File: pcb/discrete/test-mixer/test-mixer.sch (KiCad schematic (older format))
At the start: 77 parts, among them J1 UFL, J2 UFL, J3 SMA, J4 Conn_01x08, J5 Conn_01x01, J6 Conn_01x01, T1 HHM17147A1, T2 HHM17147A1, U1 ADF4360-7BCPZ, U2 BAT15-099R, X1 EC5-5032MV-100-BN-TR

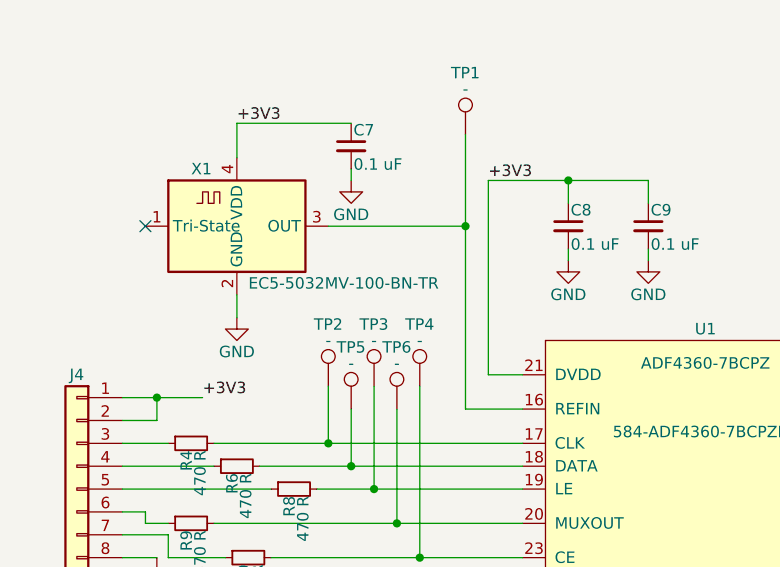
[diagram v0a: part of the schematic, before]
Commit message: Add in some more footprints before autofill
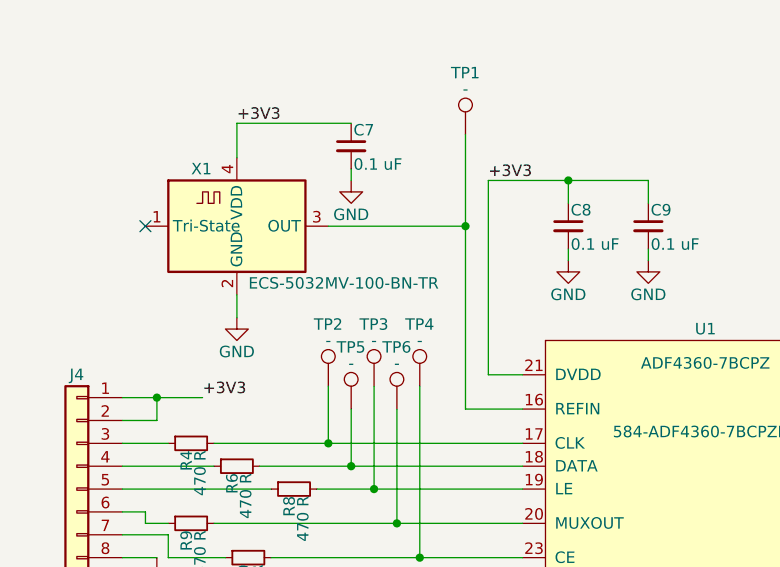
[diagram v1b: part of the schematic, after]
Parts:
- C10, C11, C2, C3, C4: footprint (none) -> Capacitor_SMD:C_0603_1608Metric_Pad1.05x0.95mm_HandSolder; Mouser (none) -> 791-RF18N101J500CT
- C12, C13, C21, C6: footprint (none) -> Capacitor_SMD:C_0402_1005Metric; Mouser (none) -> 80-C0402C103K4R7411
- C16, L10, L11, L12, L5, L6, L7, L9: footprint (none) -> Capacitor_SMD:C_0402_1005Metric; Mouser (none) -> NoPart
- C17: footprint (none) -> Capacitor_SMD:C_0402_1005Metric; Mouser (none) -> 81-GJM1555C1H3R9CB1D
- C8, C9: footprint (none) -> Capacitor_SMD:C_0402_1005Metric; Mouser (none) -> 80-C0402C104M4P
- J2: footprint (none) -> discrete_footprints:2337019-1; Mouser (none) -> 571-2337019-1
- J6: footprint (none) -> Connector_PinSocket_2.54mm:PinSocket_1x01_P2.54mm_Vertical; Mouser (none) -> NoPart
- L15: footprint (none) -> Capacitor_SMD:C_0402_1005Metric; Mouser (none) -> 815-AIML-0402-1R0KT
- L17: footprint (none) -> Capacitor_SMD:C_0402_1005Metric; Mouser (none) -> 81-LQG15HS3N9C02D
- L2: footprint (none) -> Capacitor_SMD:C_0402_1005Metric; Mouser (none) -> 81-LQG15HZ47NJ02D
- L8: footprint (none) -> Capacitor_SMD:C_0402_1005Metric; Mouser (none) -> 81-LQG15HN7N5J02D
- R10, R16, R17, R6, R8, R9: footprint (none) -> Resistor_SMD:R_0402_1005Metric; Mouser (none) -> 603-RC0402JR-13470RL
- R12, R15, R5: footprint (none) -> Resistor_SMD:R_0402_1005Metric; Mouser (none) -> NoPart
- R2: footprint (none) -> Resistor_SMD:R_0603_1608Metric_Pad1.05x0.95mm_HandSolder; Mouser (none) -> 652-CR0603-J/-3R3ELF
- R7: footprint (none) -> Resistor_SMD:R_0402_1005Metric; Mouser (none) -> 71-CRCW04020000Z0EDC
- T1: footprint (none) -> discrete_footprints:TDK_HHM17147A1
- TP1, TP3, TP4, TP5, TP6, TP7, TP8, TP9: footprint (none) -> TestPoint:TestPoint_Pad_D1.0mm; Mouser (none) -> NoPart
- X1: value EC5-5032MV-100-BN-TR -> ECS-5032MV-100-BN-TR; Mouser (none) -> 520-5032MV-100-BNT

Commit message: Autofill finish
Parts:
- L13, L14: footprint (none) -> Capacitor_SMD:C_0402_1005Metric; Mouser (none) -> 815-AIML-0402-1R0KT
- T2: footprint (none) -> discrete_footprints:TDK_HHM17147A1
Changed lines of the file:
@@
 F 0 "T2" H 9900 4150 50  0000 C CNN
 F 1 "HHM17147A1" H 9900 3650 50  0000 C CNN
-F 2 "" H 9900 4150 50  0001 C CNN
+F 2 "discrete_footprints:TDK_HHM17147A1" H 9900 4150 50  0001 C CNN
 F 3 "" H 9900 4150 50  0001 C CNN
 F 4 "810-HHM17147A1" H 9900 3550 50  0000 C CNN "Mouser"
@@
 F 0 "L14" H 6280 4340 50  0000 L CNN
 F 1 "1 uH" H 6280 4260 50  0000 L CNN
-F 2 "" H 6250 4300 50  0001 C CNN
+F 2 "Capacitor_SMD:C_0402_1005Metric" H 6250 4300 50  0001 C CNN
 F 3 "~" H 6250 4300 50  0001 C CNN
+F 4 "815-AIML-0402-1R0KT" H 6250 4300 50  0001 C CNN "Mouser"
 	1    6250 4300
 	-1   0    0    -1
@@
 F 0 "L13" H 9630 4290 50  0000 L CNN
 F 1 "1 uH" H 9630 4210 50  0000 L CNN
-F 2 "" H 9600 4250 50  0001 C CNN
+F 2 "Capacitor_SMD:C_0402_1005Metric" H 9600 4250 50  0001 C CNN
 F 3 "~" H 9600 4250 50  0001 C CNN
+F 4 "815-AIML-0402-1R0KT" H 9600 4250 50  0001 C CNN "Mouser"
 	1    9600 4250
 	1    0    0    -1

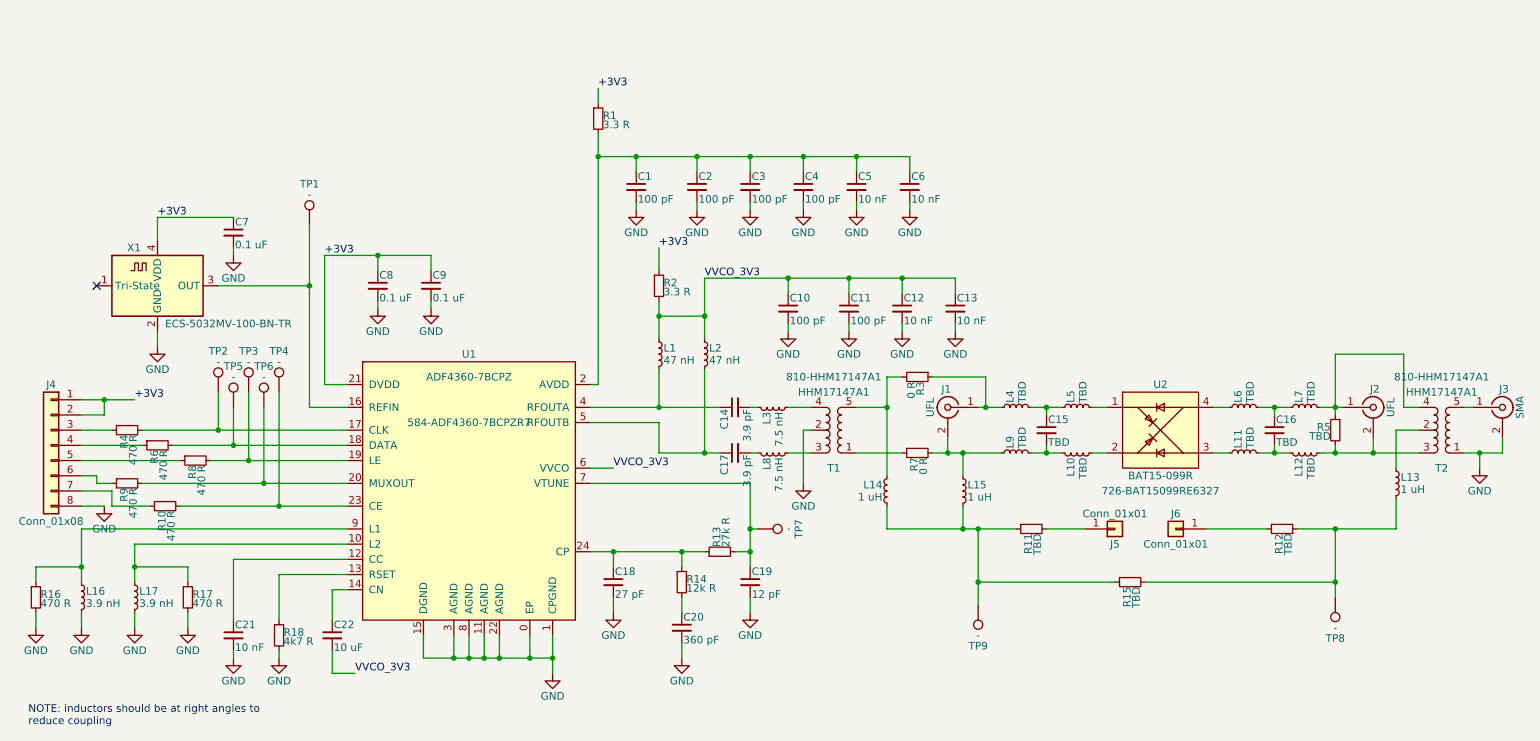
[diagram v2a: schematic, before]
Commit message: Add mounting holes, fix DRC errors
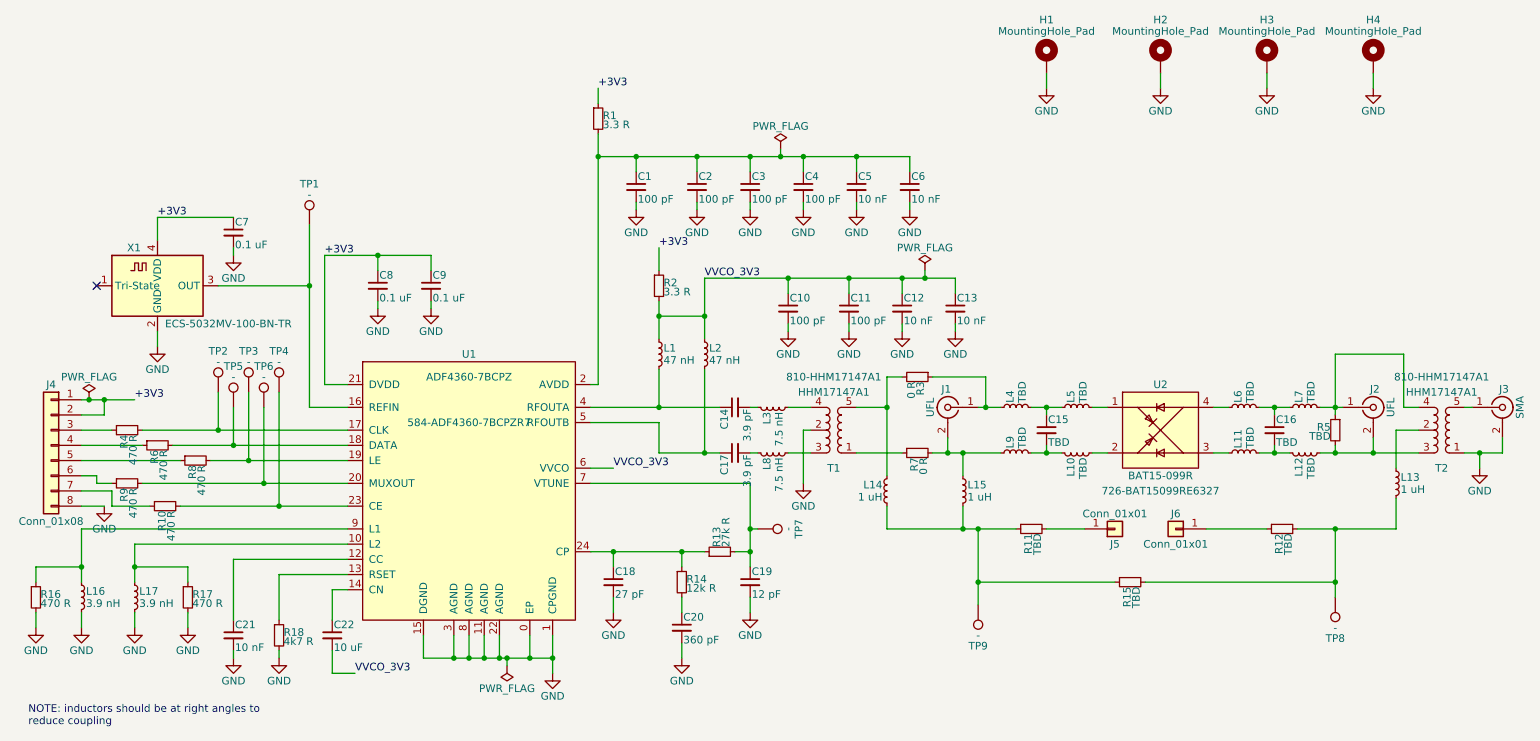
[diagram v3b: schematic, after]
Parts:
- added H1, H2, H3, H4: MountingHole_Pad, MountingHole:MountingHole_3.2mm_M3_DIN965, symbol Mechanical:MountingHole_Pad
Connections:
- net GND: now also H1.1, H2.1, H3.1, H4.1
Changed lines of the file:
@@
 	3700 5250 3700 5400
 Wire Wire Line
-	3700 5400 3900 5400
+	3700 5400 3750 5400
 Connection ~ 3900 5400
 Wire Wire Line
@@
 $EndComp
 Wire Wire Line
-	6350 2900 6700 2900
+	6350 2900 6500 2900
 Wire Wire Line
 	6700 2900 6700 3000
@@
 Connection ~ 5350 2100
 Wire Wire Line
-	5350 2100 5700 2100
+	5350 2100 5550 2100
 Wire Wire Line
 	5000 2100 5000 2200
@@
 Connection ~ 1100 3700
 Wire Wire Line
-	1100 3700 950  3700
+	1100 3700 1000 3700
 Text Label 1300 3700 0    50   ~ 0
 +3V3
@@
 Wire Wire Line
 	9200 3800 9200 3750
+$Comp
+L power:PWR_FLAG #FLG01
+U 1 1 5E1A9D94
+P 1000 3700
+F 0 "#FLG01" H 1000 3775 50  0001 C CNN
+F 1 "PWR_FLAG" H 1000 3850 50  0000 C CNN
+F 2 "" H 1000 3700 50  0001 C CNN
+F 3 "~" H 1000 3700 50  0001 C CNN
+	1    1000 3700
+	1    0    0    -1
+$EndComp
+Connection ~ 1000 3700
+Wire Wire Line
+	1000 3700 950  3700
+Wire Wire Line
+	3750 5450 3750 5400
+Connection ~ 3750 5400
+Wire Wire Line
+	3750 5400 3900 5400
+$Comp
+L power:PWR_FLAG #FLG02
+U 1 1 5E1C9779
+P 5550 2050
+F 0 "#FLG02" H 5550 2125 50  0001 C CNN
+F 1 "PWR_FLAG" H 5550 2200 50  0000 C CNN
+F 2 "" H 5550 2050 50  0001 C CNN
+F 3 "~" H 5550 2050 50  0001 C CNN
+	1    5550 2050
+	1    0    0    -1
+$EndComp
+$Comp
+L power:PWR_FLAG #FLG03
+U 1 1 5E1C9F6C
+P 6500 2850
+F 0 "#FLG03" H 6500 2925 50  0001 C CNN
+F 1 "PWR_FLAG" H 6500 3000 50  0000 C CNN
+F 2 "" H 6500 2850 50  0001 C CNN
+F 3 "~" H 6500 2850 50  0001 C CNN
+	1    6500 2850
+	1    0    0    -1
+$EndComp
+Wire Wire Line
+	5550 2050 5550 2100
+Connection ~ 5550 2100
+Wire Wire Line
+	5550 2100 5700 2100
+Wire Wire Line
+	6500 2850 6500 2900
+Connection ~ 6500 2900
+Wire Wire Line
+	6500 2900 6700 2900
+$Comp
+L Mechanical:MountingHole_Pad H1
+U 1 1 5E1EC3F2
+P 7300 1450
+F 0 "H1" H 7300 1700 50  0000 C CNN
+F 1 "MountingHole_Pad" H 7300 1625 50  0000 C CNN
+F 2 "MountingHole:MountingHole_3.2mm_M3_DIN965" H 7300 1450 50  0001 C CNN
+F 3 "~" H 7300 1450 50  0001 C CNN
+F 4 "NoPart" H 7300 1450 50  0001 C CNN "Mouser"
+	1    7300 1450
+	1    0    0    -1
+$EndComp
+$Comp
+L power:GND #PWR029
+U 1 1 5E1EED1B
+P 7300 1650
+F 0 "#PWR029" H 7300 1400 50  0001 C CNN
+F 1 "GND" H 7300 1500 50  0000 C CNN
+F 2 "" H 7300 1650 50  0001 C CNN
+F 3 "" H 7300 1650 50  0001 C CNN
+	1    7300 1650
+	1    0    0    -1
+$EndComp
+Wire Wire Line
+	7300 1650 7300 1550
+$Comp
+L Mechanical:MountingHole_Pad H2
+U 1 1 5E200292
+P 8050 1450
+F 0 "H2" H 8050 1700 50  0000 C CNN
+F 1 "MountingHole_Pad" H 8050 1625 50  0000 C CNN
+F 2 "MountingHole:MountingHole_3.2mm_M3_DIN965" H 8050 1450 50  0001 C CNN
+F 3 "~" H 8050 1450 50  0001 C CNN
+F 4 "NoPart" H 8050 1450 50  0001 C CNN "Mouser"
+	1    8050 1450
+	1    0    0    -1
+$EndComp
+$Comp
+L power:GND #PWR030
+U 1 1 5E200298
+P 8050 1650
+F 0 "#PWR030" H 8050 1400 50  0001 C CNN
+F 1 "GND" H 8050 1500 50  0000 C CNN
+F 2 "" H 8050 1650 50  0001 C CNN
+F 3 "" H 8050 1650 50  0001 C CNN
+	1    8050 1650
+	1    0    0    -1
+$EndComp
+Wire Wire Line
+	8050 1650 8050 1550
+$Comp
+L Mechanical:MountingHole_Pad H3
+U 1 1 5E210963
+P 8750 1450
+F 0 "H3" H 8750 1700 50  0000 C CNN
+F 1 "MountingHole_Pad" H 8750 1625 50  0000 C CNN
+F 2 "MountingHole:MountingHole_3.2mm_M3_DIN965" H 8750 1450 50  0001 C CNN
+F 3 "~" H 8750 1450 50  0001 C CNN
+F 4 "NoPart" H 8750 1450 50  0001 C CNN "Mouser"
+	1    8750 1450
+	1    0    0    -1
+$EndComp
+$Comp
+L power:GND #PWR031
+U 1 1 5E210969
+P 8750 1650
+F 0 "#PWR031" H 8750 1400 50  0001 C CNN
+F 1 "GND" H 8750 1500 50  0000 C CNN
+F 2 "" H 8750 1650 50  0001 C CNN
+F 3 "" H 8750 1650 50  0001 C CNN
+	1    8750 1650
+	1    0    0    -1
+$EndComp
+Wire Wire Line
+	8750 1650 8750 1550
+$Comp
+L Mechanical:MountingHole_Pad H4
+U 1 1 5E220F89
+P 9450 1450
+F 0 "H4" H 9450 1700 50  0000 C CNN
+F 1 "MountingHole_Pad" H 9450 1625 50  0000 C CNN
+F 2 "MountingHole:MountingHole_3.2mm_M3_DIN965" H 9450 1450 50  0001 C CNN
+F 3 "~" H 9450 1450 50  0001 C CNN
+F 4 "NoPart" H 9450 1450 50  0001 C CNN "Mouser"
+	1    9450 1450
+	1    0    0    -1
+$EndComp
+$Comp
+L power:GND #PWR032
+U 1 1 5E220F8F
+P 9450 1650
+F 0 "#PWR032" H 9450 1400 50  0001 C CNN
+F 1 "GND" H 9450 1500 50  0000 C CNN
+F 2 "" H 9450 1650 50  0001 C CNN
+F 3 "" H 9450 1650 50  0001 C CNN
+	1    9450 1650
+	1    0    0    -1
+$EndComp
+Wire Wire Line
+	9450 1650 9450 1550
+$Comp
+L power:PWR_FLAG #FLG0101
+U 1 1 5E2386E0
+P 3750 5450
+F 0 "#FLG0101" H 3750 5525 50  0001 C CNN
+F 1 "PWR_FLAG" H 3750 5600 50  0000 C CNN
+F 2 "" H 3750 5450 50  0001 C CNN
+F 3 "~" H 3750 5450 50  0001 C CNN
+	1    3750 5450
+	-1   0    0    1
+$EndComp
 $EndSCHEMATC

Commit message: Finish layout
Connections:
- net GND: now also T2.5 (GND); no longer T2.1 (SINGLE)
- net LO_OUT_P: now reaches C14.1, L1.2, U1.4 (RFOUTA)
- net LO_OUT_N: now reaches C17.1, L2.2, U1.5 (RFOUTB)
- net at U2.1 (A): now also L10.2; no longer L5.2
- net at U2.2 (B): now also L5.2; no longer L10.2
- net at U2.3 (C): now also L6.1; no longer L11.1
- net at U2.4 (D): now also L11.1; no longer L6.1
- net RF: now reaches J3.1 (In)
- net RF: now also T2.1 (SINGLE); no longer T2.5 (GND)
- net at J1.2 (Ext), L9.1, R7.2: no longer L15.1
- net LO_BAL_P: now reaches L14.1, R3.2, T1.5 (GND)
- net LO_BAL_N: now reaches R7.1, T1.1 (SINGLE)
- net LO_BAL_N: now also L15.1
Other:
- moved on the sheet: J3, L14, L15
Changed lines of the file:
@@
 F 4 "726-BAT15099RE6327" H 8050 3500 50  0000 C CNN "Mouser"
 	1    8050 3900
-	1    0    0    -1
+	1    0    0    1
 $EndComp
 $Comp
@@
 L Connector:Conn_Coaxial J3
 U 1 1 5DAA7992
-P 10300 3750
-F 0 "J3" H 10310 3870 50  0000 C CNN
-F 1 "SMA" V 10415 3750 50  0000 C CNN
-F 2 "discrete_footprints:142-0701-801-with-taper" H 10300 3750 50  0001 C CNN
-F 3 " ~" H 10300 3750 50  0001 C CNN
-F 4 " 530-142-0701-801 " H 10300 3750 50  0001 C CNN "Mouser"
-	1    10300 3750
-	1    0    0    -1
+P 10300 4050
+F 0 "J3" H 10310 4170 50  0000 C CNN
+F 1 "SMA" V 10415 4050 50  0000 C CNN
+F 2 "discrete_footprints:142-0701-801-with-taper" H 10300 4050 50  0001 C CNN
+F 3 " ~" H 10300 4050 50  0001 C CNN
+F 4 " 530-142-0701-801 " H 10300 4050 50  0001 C CNN "Mouser"
+	1    10300 4050
+	1    0    0    1
 $EndComp
 $Comp
@@
 F 4 "815-AIML-0402-1R0KT" H 6250 4300 50  0001 C CNN "Mouser"
 	1    6250 4300
-	-1   0    0    -1
+	1    0    0    -1
 $EndComp
 $Comp
 L Device:L_Small L15
 U 1 1 5DAB475E
-P 6750 4300
-F 0 "L15" H 6780 4340 50  0000 L CNN
-F 1 "1 uH" H 6780 4260 50  0000 L CNN
-F 2 "Capacitor_SMD:C_0402_1005Metric" H 6750 4300 50  0001 C CNN
-F 3 "~" H 6750 4300 50  0001 C CNN
-F 4 "815-AIML-0402-1R0KT" H 6750 4300 50  0001 C CNN "Mouser"
-	1    6750 4300
-	1    0    0    -1
-$EndComp
-Wire Wire Line
-	6750 4200 6750 4050
-Wire Wire Line
-	6750 4050 7000 4050
+P 6050 4300
+F 0 "L15" H 6080 4340 50  0000 L CNN
+F 1 "1 uH" H 6080 4260 50  0000 L CNN
+F 2 "Capacitor_SMD:C_0402_1005Metric" H 6050 4300 50  0001 C CNN
+F 3 "~" H 6050 4300 50  0001 C CNN
+F 4 "815-AIML-0402-1R0KT" H 6050 4300 50  0001 C CNN "Mouser"
+	1    6050 4300
+	1    0    0    -1
+$EndComp
+Wire Wire Line
+	6050 4200 6050 4050
 Wire Wire Line
 	6250 4200 6250 3750
@@
 Wire Wire Line
 	6650 3950 6650 4050
-Wire Wire Line
-	6650 4050 6750 4050
-Connection ~ 6750 4050
 $Comp
 L Device:C_Small C14
@@
 	6250 4400 6250 4550
 Wire Wire Line
-	6250 4550 6750 4550
-Wire Wire Line
-	6750 4550 6750 4400
+	6050 4550 6050 4400
 $Comp
 L Device:L_Small L13
@@
 	9200 3750 9100 3750
 Wire Wire Line
-	10100 3750 10050 3750
-Wire Wire Line
-	10300 3950 10300 4050
-Wire Wire Line
-	10300 4050 10150 4050
+	10100 4050 10050 4050
+Wire Wire Line
+	10300 3850 10300 3750
+Wire Wire Line
+	10300 3750 10150 3750
 $Comp
 L power:GND #PWR015
 U 1 1 5DAC5ECA
-P 10150 4150
-F 0 "#PWR015" H 10150 3900 50  0001 C CNN
-F 1 "GND" H 10150 4000 50  0000 C CNN
-F 2 "" H 10150 4150 50  0001 C CNN
-F 3 "" H 10150 4150 50  0001 C CNN
-	1    10150 4150
-	1    0    0    -1
-$EndComp
-Wire Wire Line
-	10150 4150 10150 4050
-Connection ~ 10150 4050
-Wire Wire Line
-	10150 4050 10050 4050
+P 10150 3650
+F 0 "#PWR015" H 10150 3400 50  0001 C CNN
+F 1 "GND" H 10150 3500 50  0000 C CNN
+F 2 "" H 10150 3650 50  0001 C CNN
+F 3 "" H 10150 3650 50  0001 C CNN
+	1    10150 3650
+	1    0    0    1
+$EndComp
+Wire Wire Line
+	10150 3650 10150 3750
+Connection ~ 10150 3750
+Wire Wire Line
+	10150 3750 10050 3750
 Wire Wire Line
 	8400 3750 8500 3750
@@
 	1    0    0    1
 $EndComp
-Connection ~ 6750 4550
 $Comp
 L Connector_Generic:Conn_01x01 J6
@@
 	6850 4900 6850 4550
 Connection ~ 6850 4550
-Wire Wire Line
-	6850 4550 6750 4550
 Text Label 2550 2750 0    50   ~ 0
 +3V3
@@
 	-1   0    0    1
 $EndComp
+Text Label 4450 3850 0    50   ~ 0
+LO_OUT_N
+Text Label 4450 3750 0    50   ~ 0
+LO_OUT_P
+Text Label 6100 3750 0    50   ~ 0
+LO_BAL_P
+Text Label 6100 4050 0    50   ~ 0
+LO_BAL_N
+Connection ~ 6050 4050
+Wire Wire Line
+	6650 4050 7000 4050
+Wire Wire Line
+	6250 4550 6850 4550
+Wire Wire Line
+	6050 4550 6250 4550
+Connection ~ 6250 4550
+Text Label 10050 4050 0    50   ~ 0
+RF
 $EndSCHEMATC
